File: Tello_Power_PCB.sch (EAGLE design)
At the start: 68 parts, among them CON1 XT30PW-F, CON2 XT30PW-F, CON3 XT30PW-F, CON4 XT30PW-F, CON5 XT30PW-F, CON6 XT30PW-M, CON7 XT60PW-M, CON8 XT30PW-F, M1 30V, M2 60V, M3 30V, M4 60V, Q1 BSS138LT3G, Q2 IPB180P04P4L02ATMA1, Q3 IPB180P04P4L02ATMA1, U1 LM3150MH/NOPB, U2 LM3150MH/NOPB, U3 LTC4357CMS8TRPBF, U4 BSC010N04LS6ATMA1, U5 BSC010N04LS6ATMA1, U6 BSC010N04LS6ATMA1

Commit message: Most things laid out
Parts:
- removed C29, C3: 10uF, rcl:C-EUC1206
- removed CON5, CON8: XT30PW-F, amass:XT30PW-F
- removed CON6: XT30PW-M, amass:XT30PW-M
- removed R12: 100R, rcl:R-US_R0603
- removed R13: 10K, rcl:R-US_R0603
- removed R5: 10k, 12v- LM3150:CRCW080510K0FKEA
- removed U4, U5, U6: BSC010N04LS6ATMA1, BSC010N04LS6ATMA1:BSC010N04LS6ATMA1
- added 2K, R15, R16: 10K, rcl:R-US_R0603
- added C30: 47nF, rcl:C-EUC0603
- added C31, C32, C33, C34, C35: 227AVG050MGBJ, 227AVG050MGBJ:227AVG050MGBJ
- added J1: PJ-002A, PJ-002A:PJ-002A
- added J2, J3, J4, J5, J6, J7, J8, J9: 1719740002, 1719740002:1719740002
- added LED1, LED2, LED3: (no value), led:LEDCHIP-LED0603
- added Q4, Q6: IXTA96P085T, IXTA96P085T:IXTA96P085T
- added R14: 1K, rcl:R-US_R0603
- added U$1, U$2: 74650073R, 74650073R:74650073R
- C1, C2: value 10uF -> 10uF 50v
- C17, C18, C19: value 25SVPF27MX -> PCR1H820MCL1GS; device 25SVPF27MX:25SVPF27MX -> PCR1H820MCL1GS:PCR1H820MCL1GS
- C4, C5, C6: value Value -> PCR1H820MCL1GS; device 12v- LM3150:CGA9P2X7R1E226M250KA -> PCR1H820MCL1GS:PCR1H820MCL1GS
- Q1: value BSS138LT3G -> BSC027N06LS5ATMA1; device BSS138LT3G:BSS138LT3G -> BSC027N06LS5ATMA1:BSC027N06LS5ATMA1
- Q2: value IPB180P04P4L02ATMA1 -> BSS138LT3G; device IPB180P04P4L02ATMA1:IPB180P04P4L02ATMA1 -> BSS138LT3G:BSS138LT3G
- Q3: value IPB180P04P4L02ATMA1 -> IXTA96P085T; device IPB180P04P4L02ATMA1:IPB180P04P4L02ATMA1 -> IXTA96P085T:IXTA96P085T
- R11: value 10K -> 33k; device rcl:R-US_R0603 -> rcl:R-US_R0805
- R4: value 191k -> 68XR10KLF; device 12v- LM3150:ERJ-6ENF1913V -> 68XR10KLF:68XR10KLF
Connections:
- removed net 12V: C15.1, C16.+, L1.2, R4.1
- removed net BATT_POSITIVE: Q2.SOURCE, Q3.SOURCE, R11.2
- removed net GATE: R12.2
- removed net N$1: Q1.D, Q2.GATE, Q3.GATE, R11.1
- removed net N$3: Q1.G, R12.1, R13.1
- removed net ROBOT_POSITIVE: Q2.DRAIN, Q3.DRAIN
- removed net VOUT: C1.1, C2.1, C29.1, C3.1, U3.OUT, U3.VDD, U4.D, U5.D, U6.D
- new net BATT_IN: 2K.1, C1.1, C2.1, Q1.D, Q3.S, Q4.S, Q6.S, U3.OUT, U3.VDD
- new net HSS_GATE: R14.2
- new net N$15: Q2.D, R15.1
- new net N_GATE: Q2.G, R14.1, R16.1
- new net P_GATES: 2K.2, C30.2, Q3.G, Q4.G, Q6.G, R15.2
- new net ROBOT_V+: C30.1, Q3.D, Q4.D, Q6.D
- new net V_ADJ: C15.1, C16.+, L1.2, R11.2
- net GND: now also Q2.S, R16.2, R4.2; no longer C17.-, C18.-, C19.-, C29.2, C3.2, C4.2, C5.2, C6.2, Q1.S, R13.2, R5.2
- net HOT_SWAP_SRC: now also Q1.S; no longer U4.S, U5.S, U6.S
- net N$26: now also R11.1, R4.1; no longer R4.2, R5.1
- net N$4: now also Q1.G; no longer U4.G, U5.G, U6.G
- net V_BATT: no longer C17.+, C18.+, C19.+, C4.1, C5.1, C6.1
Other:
- note added: "ADD BULK CAPACITANCE HERE"
- note added: "Battery High Side Switch"
- note added: "With Inrush Current Limiter"
- note removed: "High Side Switch"

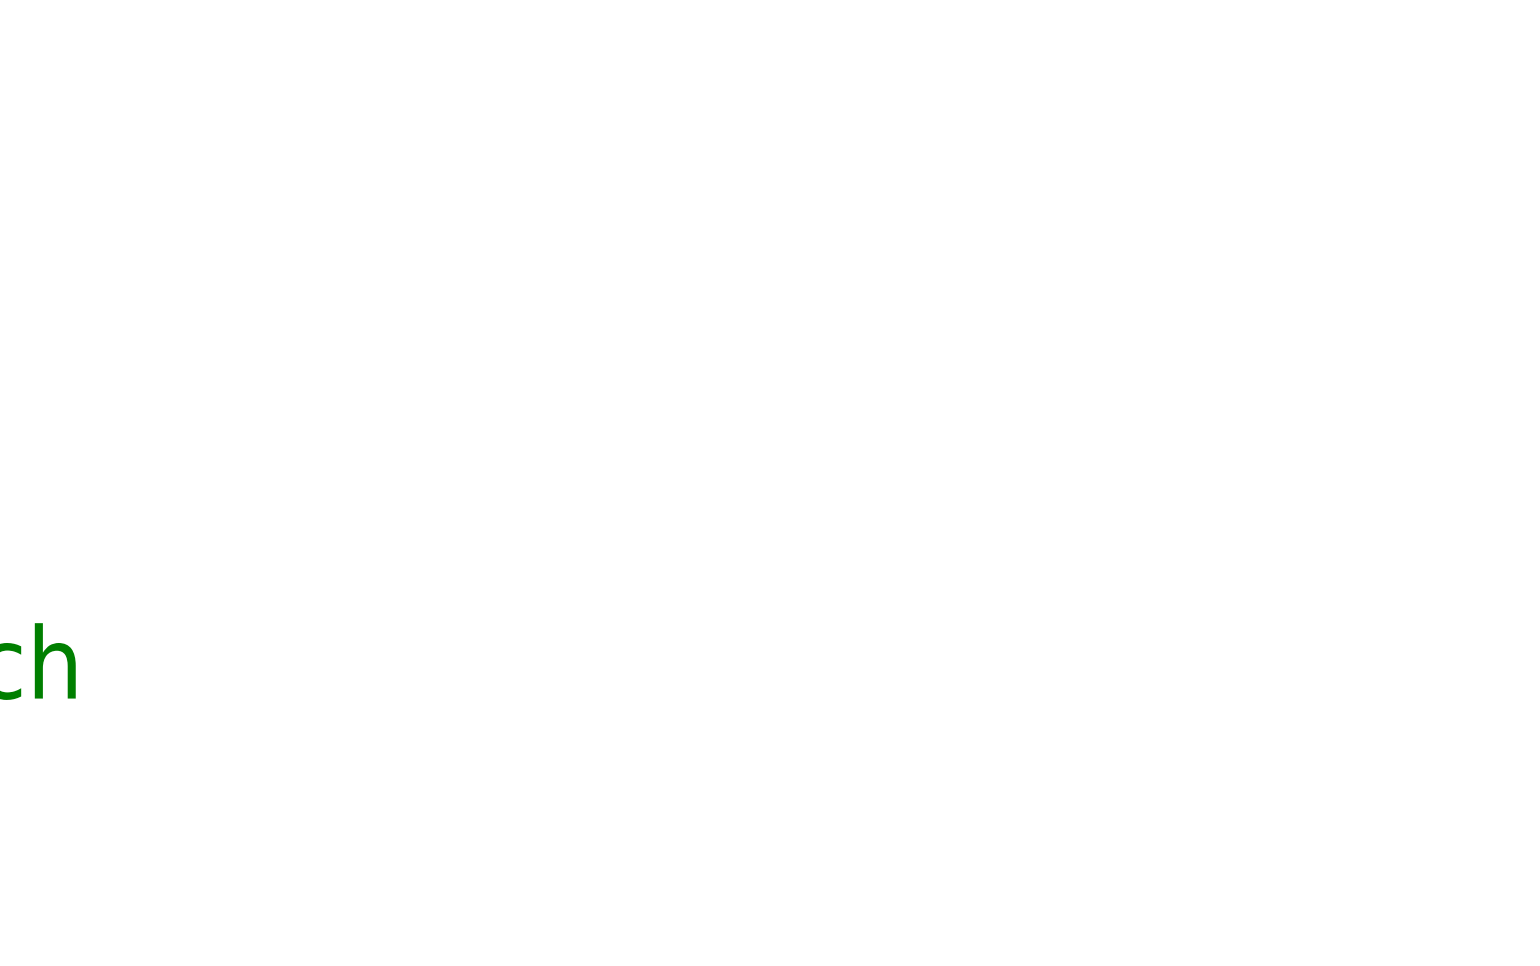
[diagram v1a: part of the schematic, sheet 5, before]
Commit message: Added motor PMOS stage
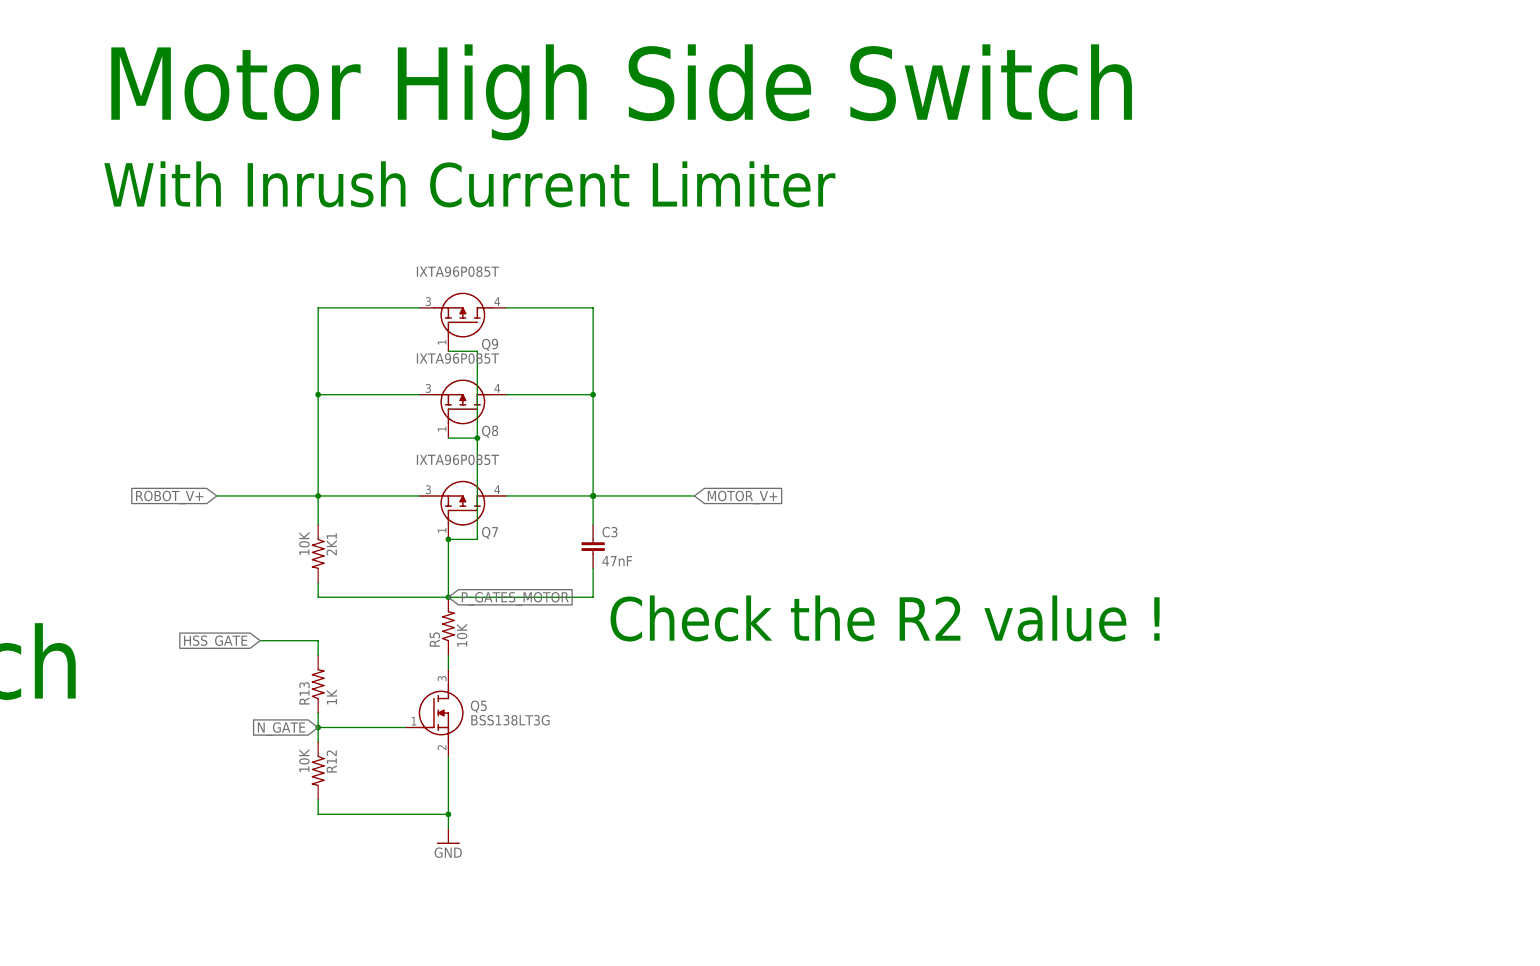
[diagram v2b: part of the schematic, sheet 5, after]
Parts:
- removed U$1, U$2: 74650073R, 74650073R:74650073R
- added 2K1, R12, R5: 10K, rcl:R-US_R0603
- added C3: 47nF, rcl:C-EUC0603
- added Q5: BSS138LT3G, BSS138LT3G:BSS138LT3G
- added Q7, Q8, Q9: IXTA96P085T, IXTA96P085T:IXTA96P085T
- added R13: 1K, rcl:R-US_R0603
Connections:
- new net MOTOR_V+: C3.1, Q7.D, Q8.D, Q9.D
- new net N$1: Q5.D, R5.1
- new net P_GATES_MOTOR: 2K1.2, C3.2, Q7.G, Q8.G, Q9.G, R5.2
- net GND: now also Q5.S, R12.2
- net HSS_GATE: now also R13.2
- net N_GATE: now also Q5.G, R12.1, R13.1
- net ROBOT_V+: now also 2K1.1, Q7.S, Q8.S, Q9.S
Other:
- note added: "Check the R2 value !"
- note added: "Motor High Side Switch"

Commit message: Routed about half of pcb
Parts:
- added U4: ADS1015IDGSR, ADS1015IDGSR:ADS1015IDGSR
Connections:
- removed net V_BATT: L3.1, L4.1
- net BATT_IN: now also CON7.+
- net GND: now also C17.2, C18.2, C19.2, C31.-, C32.-, C33.-, C34.-, C35.-, C4.2, C5.2, C6.2, CON1.-, CON2.-, CON3.-, CON4.-, CON7.-
- net MOTOR_V+: now also C31.+, C32.+, C33.+, C34.+, C35.+, CON1.+, CON2.+, CON3.+, CON4.+
- net ROBOT_V+: now also C17.1, C18.1, C19.1, C4.1, C5.1, C6.1, L3.1, L4.1
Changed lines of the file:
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@@
 <part name="C3" library="rcl" library_urn="urn:adsk.eagle:library:334" deviceset="C-EU" device="C0603" package3d_urn="urn:adsk.eagle:package:23616/2" value="47nF"/>
 <part name="R5" library="rcl" library_urn="urn:adsk.eagle:library:334" deviceset="R-US_" device="R0603" package3d_urn="urn:adsk.eagle:package:23555/3" value="10K"/>
+<part name="FRAME11" library="frames" library_urn="urn:adsk.eagle:library:229" deviceset="FRAME_A_L" device=""/>
+<part name="FRAME12" library="frames" library_urn="urn:adsk.eagle:library:229" deviceset="FRAME_B_L" device=""/>
+<part name="U4" library="ADS1015IDGSR" deviceset="ADS1015IDGSR" device=""/>
 </parts>
 <sheets>
@@
 </busses>
 <nets>
+<net name="MOTOR_V+" class="0">
+<segment>
+<pinref part="C31" gate="G$1" pin="+"/>
+<wire x1="33.02" y1="43.18" x2="25.4" y2="43.18" width="0.1524" layer="91"/>
+<pinref part="C32" gate="G$1" pin="+"/>
+<wire x1="33.02" y1="43.18" x2="43.18" y2="43.18" width="0.1524" layer="91"/>
+<junction x="33.02" y="43.18"/>
+<pinref part="C33" gate="G$1" pin="+"/>
+<wire x1="43.18" y1="43.18" x2="53.34" y2="43.18" width="0.1524" layer="91"/>
+<junction x="43.18" y="43.18"/>
+<pinref part="C34" gate="G$1" pin="+"/>
+<wire x1="53.34" y1="43.18" x2="63.5" y2="43.18" width="0.1524" layer="91"/>
+<junction x="53.34" y="43.18"/>
+<pinref part="C35" gate="G$1" pin="+"/>
+<wire x1="63.5" y1="43.18" x2="73.66" y2="43.18" width="0.1524" layer="91"/>
+<junction x="63.5" y="43.18"/>
+<label x="25.4" y="43.18" size="1.778" layer="95" rot="R180" xref="yes"/>
+</segment>
+<segment>
+<pinref part="CON1" gate="G$1" pin="+"/>
+<wire x1="381" y1="170.18" x2="365.76" y2="170.18" width="0.1524" layer="91"/>
+<wire x1="365.76" y1="170.18" x2="365.76" y2="149.86" width="0.1524" layer="91"/>
+<pinref part="CON2" gate="G$1" pin="+"/>
+<wire x1="365.76" y1="149.86" x2="381" y2="149.86" width="0.1524" layer="91"/>
+<wire x1="365.76" y1="149.86" x2="365.76" y2="132.08" width="0.1524" layer="91"/>
+<junction x="365.76" y="149.86"/>
+<pinref part="CON3" gate="G$1" pin="+"/>
+<wire x1="365.76" y1="132.08" x2="381" y2="132.08" width="0.1524" layer="91"/>
+<wire x1="365.76" y1="132.08" x2="365.76" y2="114.3" width="0.1524" layer="91"/>
+<junction x="365.76" y="132.08"/>
+<pinref part="CON4" gate="G$1" pin="+"/>
+<wire x1="365.76" y1="114.3" x2="381" y2="114.3" width="0.1524" layer="91"/>
+<wire x1="365.76" y1="114.3" x2="365.76" y2="109.22" width="0.1524" layer="91"/>
+<junction x="365.76" y="114.3"/>
+<label x="365.76" y="109.22" size="1.778" layer="95" rot="R270" xref="yes"/>
+</segment>
+</net>
+<net name="GND" class="0">
+<segment>
+<pinref part="C35" gate="G$1" pin="-"/>
+<pinref part="C34" gate="G$1" pin="-"/>
+<wire x1="73.66" y1="30.48" x2="63.5" y2="30.48" width="0.1524" layer="91"/>
+<pinref part="C33" gate="G$1" pin="-"/>
+<wire x1="63.5" y1="30.48" x2="53.34" y2="30.48" width="0.1524" layer="91"/>
+<junction x="63.5" y="30.48"/>
+<pinref part="C32" gate="G$1" pin="-"/>
+<wire x1="53.34" y1="30.48" x2="43.18" y2="30.48" width="0.1524" layer="91"/>
+<junction x="53.34" y="30.48"/>
+<pinref part="C31" gate="G$1" pin="-"/>
+<wire x1="43.18" y1="30.48" x2="33.02" y2="30.48" width="0.1524" layer="91"/>
+<junction x="43.18" y="30.48"/>
+<wire x1="33.02" y1="30.48" x2="25.4" y2="30.48" width="0.1524" layer="91"/>
+<junction x="33.02" y="30.48"/>
+<label x="25.4" y="30.48" size="1.778" layer="95" rot="R180" xref="yes"/>
+</segment>
+<segment>
+<pinref part="CON4" gate="G$1" pin="-"/>
+<wire x1="381" y1="119.38" x2="358.14" y2="119.38" width="0.1524" layer="91"/>
+<pinref part="CON3" gate="G$1" pin="-"/>
+<wire x1="381" y1="137.16" x2="358.14" y2="137.16" width="0.1524" layer="91"/>
+<wire x1="358.14" y1="137.16" x2="358.14" y2="119.38" width="0.1524" layer="91"/>
+<wire x1="358.14" y1="119.38" x2="358.14" y2="109.22" width="0.1524" layer="91"/>
+<junction x="358.14" y="119.38"/>
+<pinref part="CON2" gate="G$1" pin="-"/>
+<wire x1="381" y1="154.94" x2="358.14" y2="154.94" width="0.1524" layer="91"/>
+<wire x1="358.14" y1="154.94" x2="358.14" y2="137.16" width="0.1524" layer="91"/>
+<junction x="358.14" y="137.16"/>
+<pinref part="CON1" gate="G$1" pin="-"/>
+<wire x1="381" y1="175.26" x2="358.14" y2="175.26" width="0.1524" layer="91"/>
+<wire x1="358.14" y1="175.26" x2="358.14" y2="154.94" width="0.1524" layer="91"/>
+<junction x="358.14" y="154.94"/>
+<label x="358.14" y="109.22" size="1.778" layer="95" rot="R270" xref="yes"/>
+</segment>
+<segment>
+<pinref part="CON7" gate="G$1" pin="-"/>
+<wire x1="27.94" y1="236.22" x2="30.48" y2="236.22" width="0.1524" layer="91"/>
+<label x="30.48" y="236.22" size="1.778" layer="95" xref="yes"/>
+</segment>
+</net>
+<net name="BATT_IN" class="0">
+<segment>
+<pinref part="CON7" gate="G$1" pin="+"/>
+<wire x1="27.94" y1="241.3" x2="30.48" y2="241.3" width="0.1524" layer="91"/>
+<label x="30.48" y="241.3" size="1.778" layer="95" xref="yes"/>
+</segment>
+</net>
 </nets>
 </sheet>
@@
 <wire x1="186.69" y1="105.41" x2="186.69" y2="104.14" width="0.1524" layer="91"/>
 <junction x="186.69" y="105.41"/>
+</segment>
+<segment>
+<pinref part="C19" gate="A" pin="2"/>
+<pinref part="C18" gate="A" pin="2"/>
+<wire x1="106.68" y1="121.92" x2="96.52" y2="121.92" width="0.1524" layer="91"/>
+<pinref part="C17" gate="A" pin="2"/>
+<wire x1="96.52" y1="121.92" x2="86.36" y2="121.92" width="0.1524" layer="91"/>
+<junction x="96.52" y="121.92"/>
+<pinref part="C6" gate="A" pin="2"/>
+<wire x1="86.36" y1="121.92" x2="76.2" y2="121.92" width="0.1524" layer="91"/>
+<junction x="86.36" y="121.92"/>
+<pinref part="C5" gate="A" pin="2"/>
+<wire x1="76.2" y1="121.92" x2="66.04" y2="121.92" width="0.1524" layer="91"/>
+<junction x="76.2" y="121.92"/>
+<pinref part="C4" gate="A" pin="2"/>
+<wire x1="66.04" y1="121.92" x2="55.88" y2="121.92" width="0.1524" layer="91"/>
+<junction x="66.04" y="121.92"/>
+<junction x="55.88" y="121.92"/>
+<wire x1="55.88" y1="121.92" x2="50.8" y2="121.92" width="0.1524" layer="91"/>
+<label x="50.8" y="121.92" size="1.778" layer="95" rot="R180" xref="yes"/>
 </segment>
 </net>
@@
 </segment>
 </net>
-<net name="V_BATT" class="0">
-<segment>
-<pinref part="L4" gate="A" pin="1"/>
-<label x="53.34" y="217.17" size="3.81" layer="95" rot="R180" xref="yes"/>
-<wire x1="85.09" y1="218.44" x2="71.12" y2="218.44" width="0.1524" layer="91"/>
-<wire x1="71.12" y1="218.44" x2="53.34" y2="218.44" width="0.1524" layer="91"/>
-<wire x1="71.12" y1="200.66" x2="71.12" y2="218.44" width="0.1524" layer="91"/>
-<junction x="71.12" y="218.44"/>
-</segment>
-</net>
 <net name="N$7" class="0">
 <segment>
@@
 <pinref part="U2" gate="A" pin="FB"/>
 <wire x1="223.52" y1="104.14" x2="223.52" y2="114.3" width="0.1524" layer="91"/>
+</segment>
+</net>
+<net name="ROBOT_V+" class="0">
+<segment>
+<pinref part="C19" gate="A" pin="1"/>
+<pinref part="C18" gate="A" pin="1"/>
+<wire x1="106.68" y1="129.54" x2="96.52" y2="129.54" width="0.1524" layer="91"/>
+<pinref part="C17" gate="A" pin="1"/>
+<wire x1="96.52" y1="129.54" x2="86.36" y2="129.54" width="0.1524" layer="91"/>
+<junction x="96.52" y="129.54"/>
+<pinref part="C6" gate="A" pin="1"/>
+<wire x1="86.36" y1="129.54" x2="76.2" y2="129.54" width="0.1524" layer="91"/>
+<junction x="86.36" y="129.54"/>
+<pinref part="C5" gate="A" pin="1"/>
+<wire x1="76.2" y1="129.54" x2="66.04" y2="129.54" width="0.1524" layer="91"/>
+<junction x="76.2" y="129.54"/>
+<pinref part="C4" gate="A" pin="1"/>
+<wire x1="66.04" y1="129.54" x2="55.88" y2="129.54" width="0.1524" layer="91"/>
+<junction x="66.04" y="129.54"/>
+<wire x1="55.88" y1="129.54" x2="50.8" y2="129.54" width="0.1524" layer="91"/>
+<junction x="55.88" y="129.54"/>
+<label x="50.8" y="129.54" size="1.778" layer="95" rot="R180" xref="yes"/>
+</segment>
+<segment>
+<pinref part="L4" gate="A" pin="1"/>
+<label x="53.34" y="217.17" size="3.81" layer="95" rot="R180" xref="yes"/>
+<wire x1="85.09" y1="218.44" x2="71.12" y2="218.44" width="0.1524" layer="91"/>
+<wire x1="71.12" y1="218.44" x2="53.34" y2="218.44" width="0.1524" layer="91"/>
+<wire x1="71.12" y1="200.66" x2="71.12" y2="218.44" width="0.1524" layer="91"/>
+<junction x="71.12" y="218.44"/>
 </segment>
 </net>
@@
 </segment>
 </net>
-<net name="V_BATT" class="0">
+<net name="ROBOT_V+" class="0">
 <segment>
 <pinref part="L3" gate="G$1" pin="1"/>
@@
 </nets>
 </sheet>
+<sheet>
+<plain>
+</plain>
+<instances>
+<instance part="FRAME11" gate="G$2" x="325.12" y="0" smashed="yes">
+<attribute name="LAST_DATE_TIME" x="337.82" y="1.27" size="2.54" layer="94"/>
+<attribute name="SHEET" x="411.48" y="1.27" size="2.54" layer="94"/>
+<attribute name="DRAWING_NAME" x="342.9" y="19.05" size="2.54" layer="94"/>
+</instance>
+<instance part="FRAME12" gate="G$1" x="0" y="0" smashed="yes"/>
+<instance part="U4" gate="A" x="88.9" y="83.82" smashed="yes">
+<attribute name="NAME" x="76.2" y="102.6" size="2.0828" layer="95" ratio="10" rot="SR0"/>
+<attribute name="VALUE" x="76.2" y="62.04" size="2.0828" layer="96" ratio="10" rot="SR0"/>
+</instance>
+</instances>
+<busses>
+</busses>
+<nets>
+</nets>
+</sheet>

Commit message: Made big changes to power distr.
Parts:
- removed Q4, Q6: IXTA96P085T, IXTA96P085T:IXTA96P085T
- removed Q5: BSS138LT3G, BSS138LT3G:BSS138LT3G
- added C29, C36: 10uF 50v, rcl:C-EUC1206
- added CR2: STPS1150A, STPS1150A:STPS1150A
- added R18: 68XR10KLF, 68XR10KLF:68XR10KLF
- added R19, R22: 10K, rcl:R-US_R0603
- added R21, R25: (no value), rcl:R-US_R0603
- added R29: 1.8K, rcl:R-US_R0603
- added R30: 1.62K, rcl:R-US_R0603
- added U11: TLV7041DCKR, TLV7041DCKR:TLV7041DCKR
- added U12, U6, U7: DMN67D8LW-13, DMN67D8LW-13:DMN67D8LW-13
- added U5: MIC5282-3.3YMM-TR, MIC5282-3-3YMM:MIC5282-3.3YMM-TR
- added U8: LTC4357CMS8TRPBF, LTC4357:LTC4357CMS8TRPBF
- added U9: TLV6713DDCTDDC0006A_M, TLV6713DDC:TLV6713DDCTDDC0006A_M
- Q2: value BSS138LT3G -> BSC027N06LS5ATMA1; device BSS138LT3G:BSS138LT3G -> BSC027N06LS5ATMA1:BSC027N06LS5ATMA1
- R27, R28: value 10K -> 2K
- renumbered 2K to R27, 2K1 to R28
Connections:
- removed net HOT_SWAP_SRC: CR1.1, Q1.S, U3.IN
- removed net HSS_GATE: R13.2, R14.2
- new net 5V_ALWAYS_ON: R13.2, R14.2, R25.2, U9.VCC
- new net N$16: Q2.G, U8.GATE
- new net N$3: R19.1, R29.2, U11.IN+
- new net N$6: R22.1, R30.2, U11.IN-
- new net N$8: R18.1, R21.1, U9.SENSE
- new net N_GATE_M: R12.1, R13.1, U7.G
- new net PS_IN: CR1.1, Q1.S, R19.2, U3.IN
- new net PS_SV_COMP: R25.1, U11.OUT, U12.G
- new net SYSTEM_IN: C1.1, C2.1, C29.1, C36.1, Q1.D, Q2.D, Q3.S, R27.1, U3.OUT, U3.VDD, U8.OUT, U8.VDD
- new net SYSTEM_SWITCHED: C30.1, L3.1, L4.1, Q3.D
- new net SYS_UV_SOURCE: U12.S, U9.OUT
- new net S_N_GATE: U12.D
- net BATT_IN: now also CR2.1, J2.2, J3.2, J8.2, J9.2, Q2.S, Q7.S, Q8.S, Q9.S, R21.2, R22.2, R28.1, U8.IN; no longer C1.1, C2.1, Q1.D, Q3.S, Q4.S, Q6.S, R27.1, U3.OUT, U3.VDD
- net GND: now also C29.2, C36.2, CR2.2, R18.2, R29.1, R30.1, U6.S, U7.S, U8.GND, U9.GND; no longer Q2.S, Q5.S
- net N$1: now also U7.D; no longer Q5.D
- net N$15: now also U6.D; no longer Q2.D
- net N_GATE: now also U6.G; no longer Q2.G, Q5.G, R12.1, R13.1
- net P_GATES: no longer Q4.G, Q6.G
- net ROBOT_V+: no longer C30.1, L3.1, L4.1, Q3.D, Q4.D, Q6.D, Q7.S, Q8.S, Q9.S, R28.1
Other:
- note added: "System Under Voltage"
- note added: "This circuit ensures that the system under voltage only applies if power supply voltage is lower than battery voltage"
